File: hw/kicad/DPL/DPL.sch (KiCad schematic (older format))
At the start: 1 part

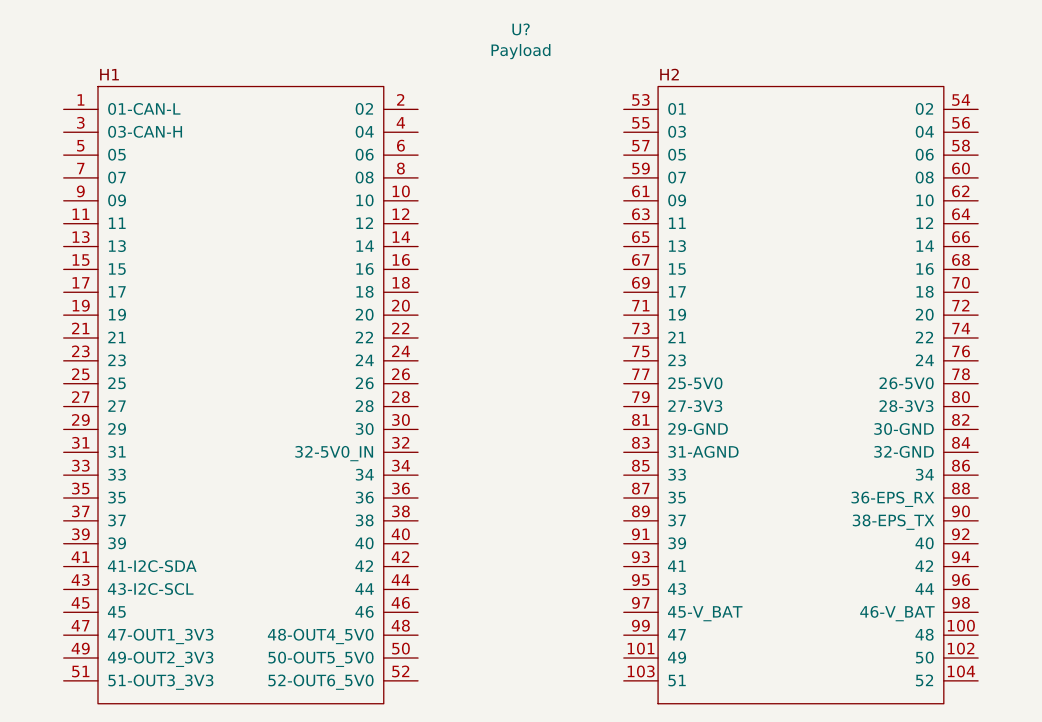
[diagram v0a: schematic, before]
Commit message: Added some net names.
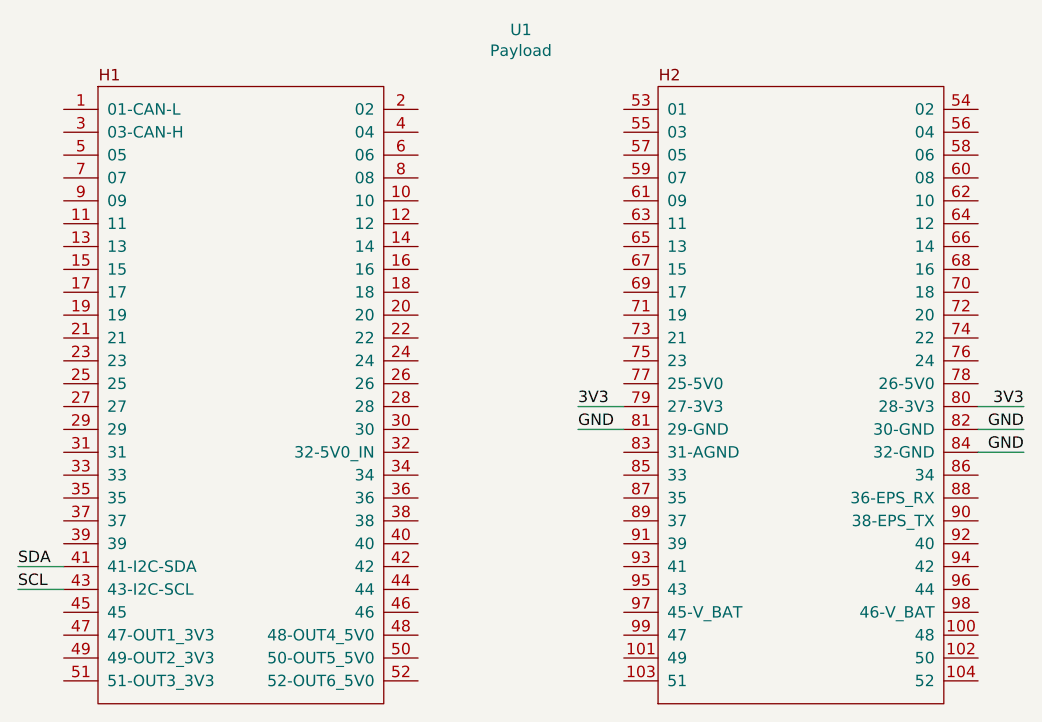
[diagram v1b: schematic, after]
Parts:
- gave numbers to parts that had none: 1
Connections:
- net SDA: now reaches U1.41 (41-I2C-SDA)
- net SCL: now reaches U1.43 (43-I2C-SCL)
- net 3V3: now reaches U1.79 (27-3V3)
- net 3V3: now also U1.80 (28-3V3)
- net GND: now reaches U1.81 (29-GND)
- net GND: now also U1.82 (30-GND), U1.84 (32-GND)
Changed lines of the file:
@@
 EESchema Schematic File Version 4
+LIBS:DPL-cache
 EELAYER 29 0
 EELAYER END
@@
 $EndDescr
 $Comp
-L Payload:Payload U?
+L Payload:Payload U1
 U 1 1 5C059BEE
 P 5950 3250
-F 0 "U?" H 5950 4798 50  0000 C CNN
+F 0 "U1" H 5950 4798 50  0000 C CNN
 F 1 "Payload" H 5950 4707 50  0000 C CNN
 F 2 "" H 4850 4050 50  0001 C CNN
@@
 	1    0    0    -1
 $EndComp
+Text Label 6200 3450 0    50   ~ 0
+GND
+Text Label 8150 3450 2    50   ~ 0
+GND
+Text Label 8150 3550 2    50   ~ 0
+GND
+Wire Wire Line
+	8150 3450 7950 3450
+Wire Wire Line
+	7950 3550 8150 3550
+Wire Wire Line
+	6400 3450 6200 3450
+Text Label 6200 3350 0    50   ~ 0
+3V3
+Text Label 8150 3350 2    50   ~ 0
+3V3
+Wire Wire Line
+	8150 3350 7950 3350
+Wire Wire Line
+	6400 3350 6200 3350
+Text Label 3750 4050 0    50   ~ 0
+SDA
+Text Label 3750 4150 0    50   ~ 0
+SCL
+Wire Wire Line
+	3950 4050 3750 4050
+Wire Wire Line
+	3750 4150 3950 4150
 $EndSCHEMATC

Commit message: Update.
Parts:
- added C? (x2): 22pF, symbol Device:C
- added C?: 100nF, symbol Device:C
- added J?: DPL1, symbol Connector:Screw_Terminal_01x02
- added J?: DPL2, symbol Connector:Screw_Terminal_01x02
- added J?: DPL3, symbol Connector:Screw_Terminal_01x02
- added J?: DPL4, symbol Connector:Screw_Terminal_01x02
- added J?: DPL5, symbol Connector:Screw_Terminal_01x02
- added J?: DPL6, symbol Connector:Screw_Terminal_01x02
- added R?: 10k, symbol Device:R
- added U?: ATmega328-PU, Package_DIP:DIP-28_W7.62mm, symbol MCU_Microchip_ATmega:ATmega328-PU
- added Y?: 8MHz, symbol Device:Crystal
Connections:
- net 3V3: now also R?.1, U?.20 (AVCC), U?.7 (VCC)
- net GND: now also C?.2, C?.2, J?.2 (Pin_2), J?.2 (Pin_2), J?.2 (Pin_2), J?.2 (Pin_2), J?.2 (Pin_2), J?.2 (Pin_2), U?.22 (GND), U?.8 (GND)
- new net DTR: C?.2
- new net MISO: U?.18 (PB4)
- new net MOSI: U?.17 (PB3)
- new net RESET: C?.1, R?.2, U?.1 (~RESET~/PC6)
- new net SCK: U?.19 (PB5)
- new net XTAL1: C?.1, U?.9 (XTAL1/PB6), Y?.2
- new net XTAL2: C?.1, U?.10 (XTAL2/PB7), Y?.1
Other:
- moved on the sheet: U1

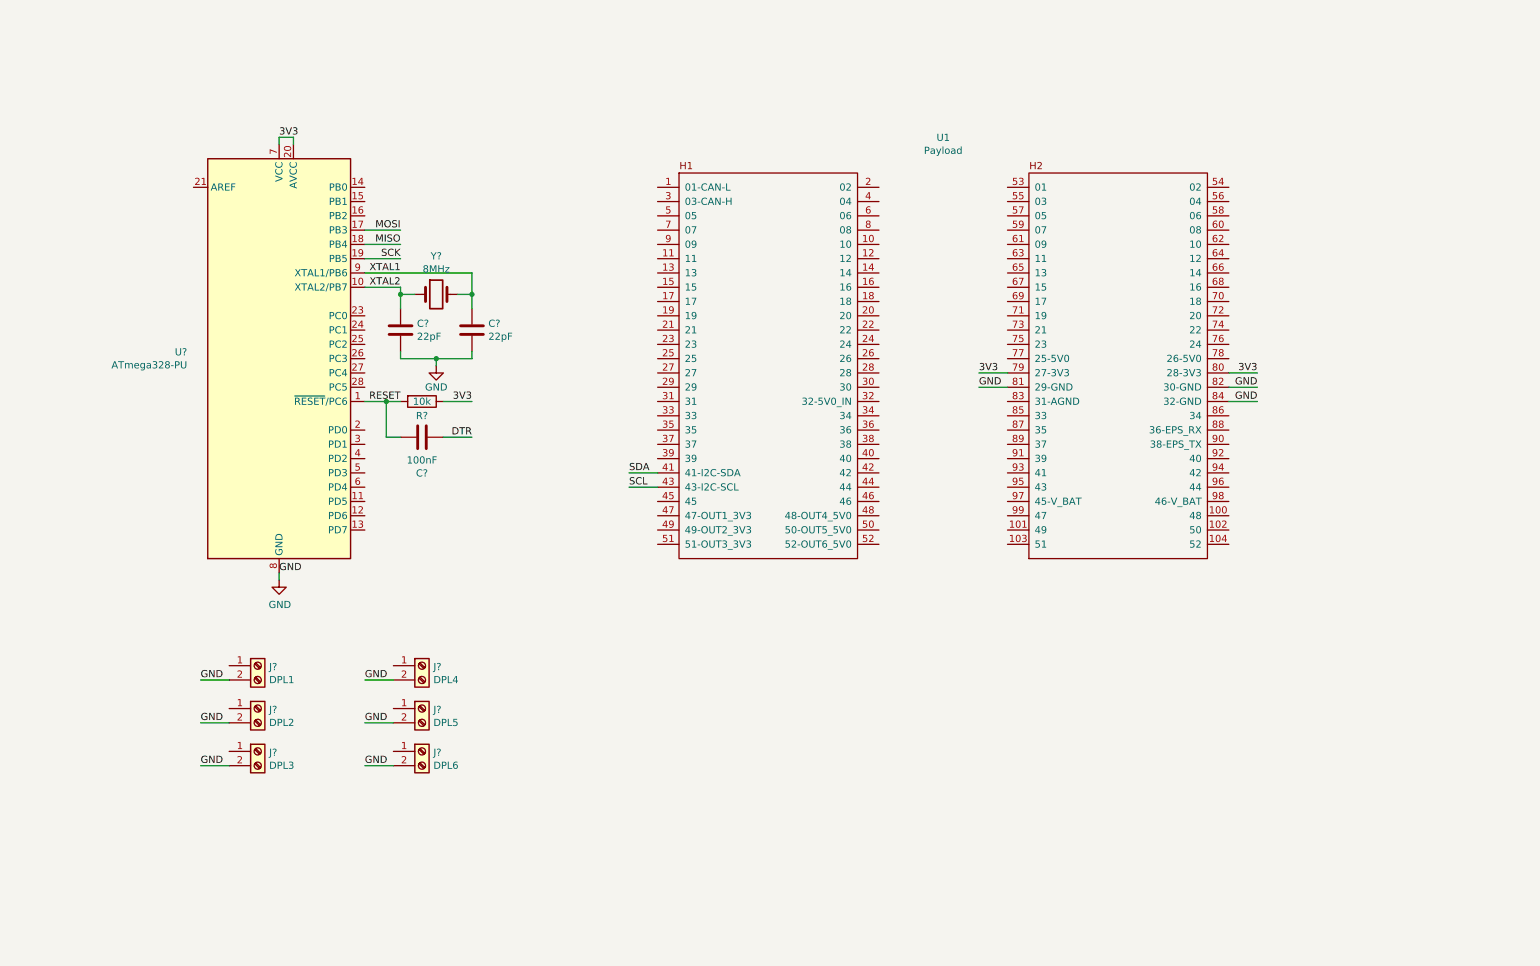
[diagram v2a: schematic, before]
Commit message: Changed the ATMEGA328 with the SAMD21E.
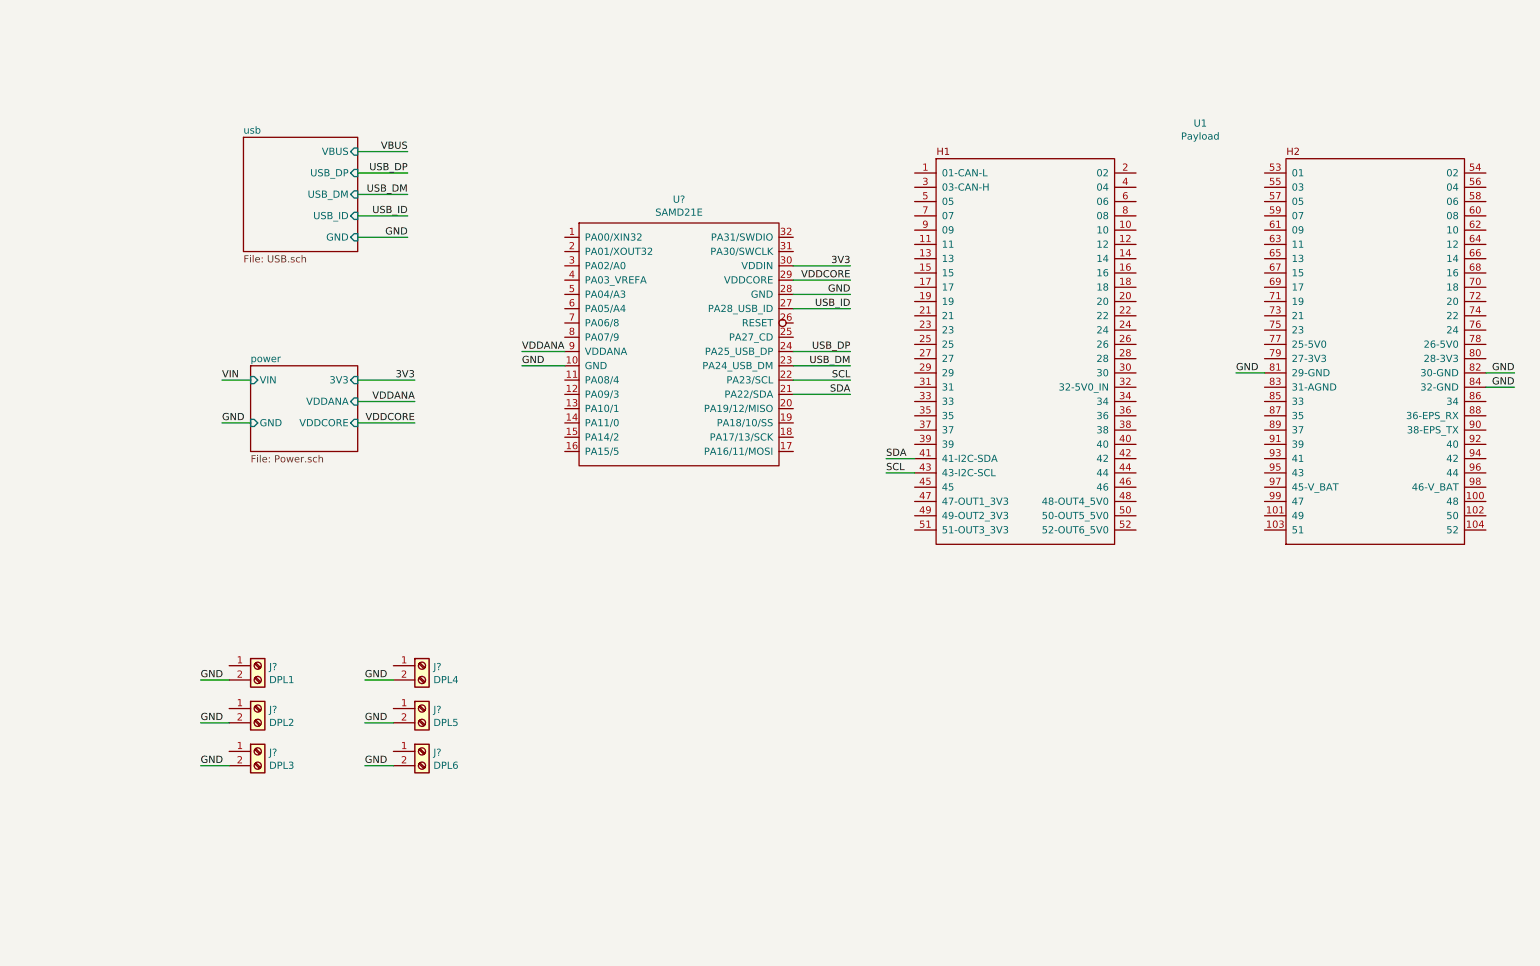
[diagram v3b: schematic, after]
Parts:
- removed C? (x2): 22pF, symbol Device:C
- removed C?: 100nF, symbol Device:C
- removed R?: 10k, symbol Device:R
- removed U?: ATmega328-PU, Package_DIP:DIP-28_W7.62mm, symbol MCU_Microchip_ATmega:ATmega328-PU
- removed Y?: 8MHz, symbol Device:Crystal
- added U?: SAMD21E, symbol Arduino:SAMD21E
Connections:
- net 3V3: now also U?.30 (VDDIN); no longer U1.79 (27-3V3), U1.80 (28-3V3)
- net GND: now also U?.10 (GND), U?.28 (GND)
- net SCL: now also U?.22 (PA23/SCL)
- net SDA: now also U?.21 (PA22/SDA)
- new net USB_DM: U?.23 (PA24_USB_DM)
- new net USB_DP: U?.24 (PA25_USB_DP)
- new net USB_ID: U?.27 (PA28_USB_ID)
- new net VDDANA: U?.9 (VDDANA)
- new net VDDCORE: U?.29 (VDDCORE)
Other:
- moved on the sheet: U1

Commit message: Added transistors for the deployment system. Updated the microcontroller's symbol.
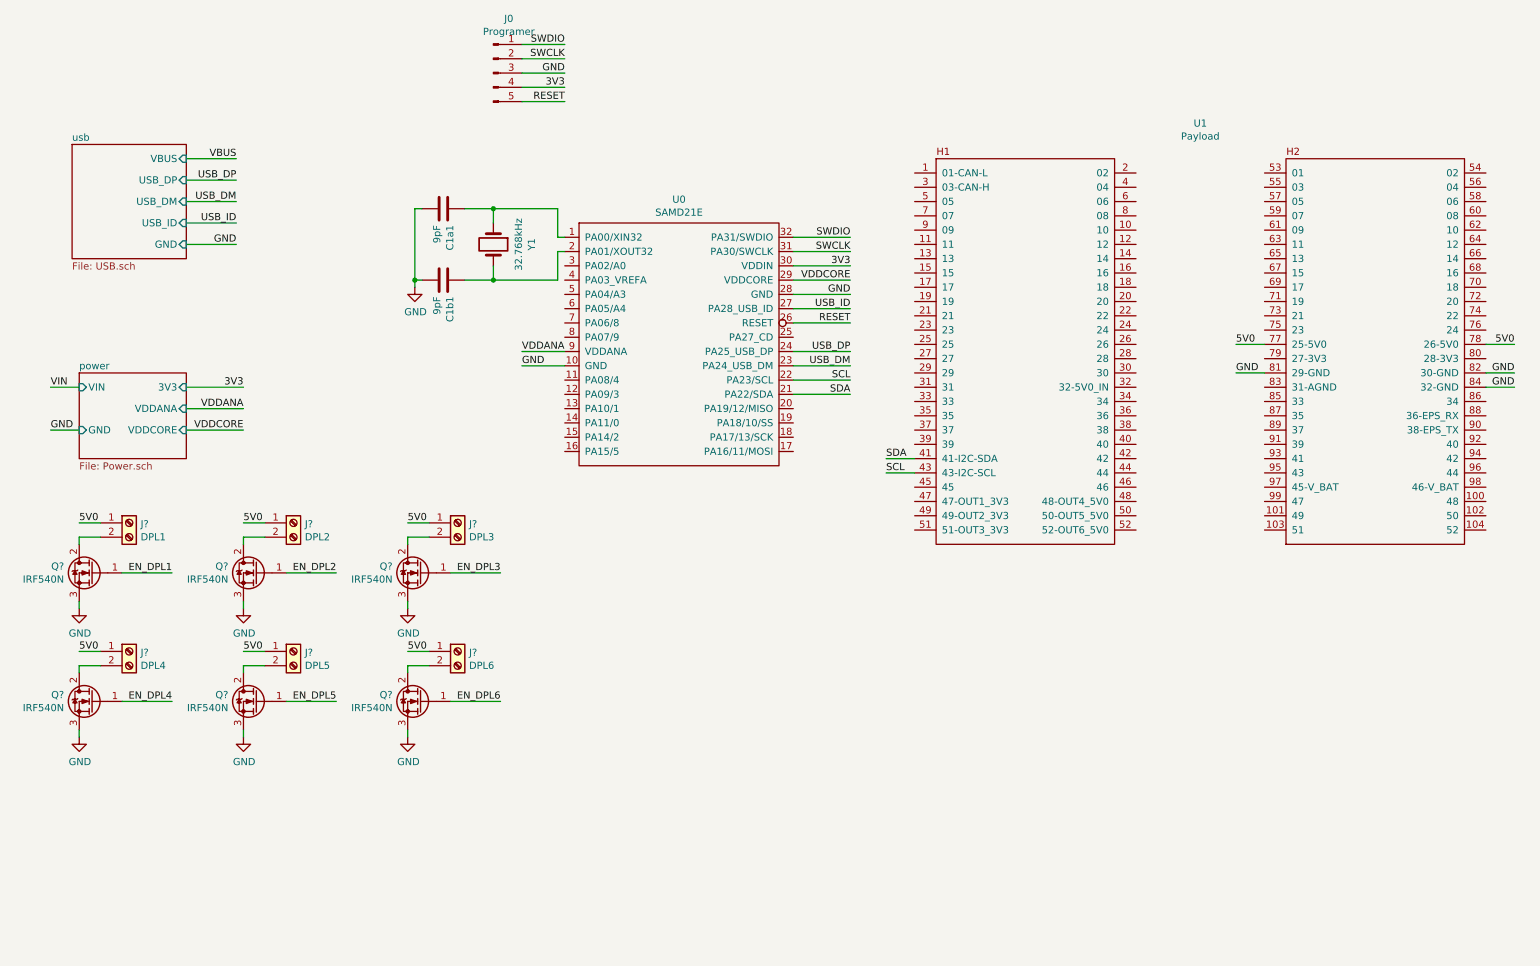
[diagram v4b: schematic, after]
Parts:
- removed U?: SAMD21E, symbol Arduino:SAMD21E
- added C1a1, C1b1: 9pF, symbol Device:C
- added J0: Programer, symbol Connector:Conn_01x05_Male
- added Q? (x6): IRF540N, Package_TO_SOT_THT:TO-220-3_Vertical, symbol Transistor_FET:IRF540N
- added U0: SAMD21E, symbol Arduino:SAMD21E
- added Y1: 32.768kHz, symbol Device:Crystal
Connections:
- net 3V3: now also J0.4 (Pin_4), U0.30 (VDDIN)
- net GND: now also C1a1.2, C1b1.2, J0.3 (Pin_3), Q?.3 (S), Q?.3 (S), Q?.3 (S), Q?.3 (S), Q?.3 (S), Q?.3 (S), U0.10 (GND), U0.28 (GND); no longer J?.2 (Pin_2), J?.2 (Pin_2), J?.2 (Pin_2), J?.2 (Pin_2), J?.2 (Pin_2), J?.2 (Pin_2)
- net SCL: now also U0.22 (PA23/SCL)
- net SDA: now also U0.21 (PA22/SDA)
- net USB_DM: now also U0.23 (PA24_USB_DM)
- net USB_DP: now also U0.24 (PA25_USB_DP)
- net USB_ID: now also U0.27 (PA28_USB_ID)
- net VDDANA: now also U0.9 (VDDANA)
- net VDDCORE: now also U0.29 (VDDCORE)
- net 5V0: now reaches U1.77 (25-5V0)
- net 5V0: now also J?.1 (Pin_1), J?.1 (Pin_1), J?.1 (Pin_1), J?.1 (Pin_1), J?.1 (Pin_1), J?.1 (Pin_1), U1.78 (26-5V0)
- new net: J?.2 (Pin_2), Q?.2 (D) (x6)
- new net: C1a1.1, U0.1 (PA00/XIN32), Y1.1
- new net: C1b1.1, U0.2 (PA01/XOUT32), Y1.2
- new net EN_DPL1: Q?.1 (G)
- new net EN_DPL2: Q?.1 (G)
- new net EN_DPL3: Q?.1 (G)
- new net EN_DPL4: Q?.1 (G)
- new net EN_DPL5: Q?.1 (G)
- new net EN_DPL6: Q?.1 (G)
- new net RESET: J0.5 (Pin_5), U0.26 (RESET)
- new net SWCLK: J0.2 (Pin_2), U0.31 (PA30/SWCLK)
- new net SWDIO: J0.1 (Pin_1), U0.32 (PA31/SWDIO)
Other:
- moved on the sheet: J?

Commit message: Added reed switches to the schematic.
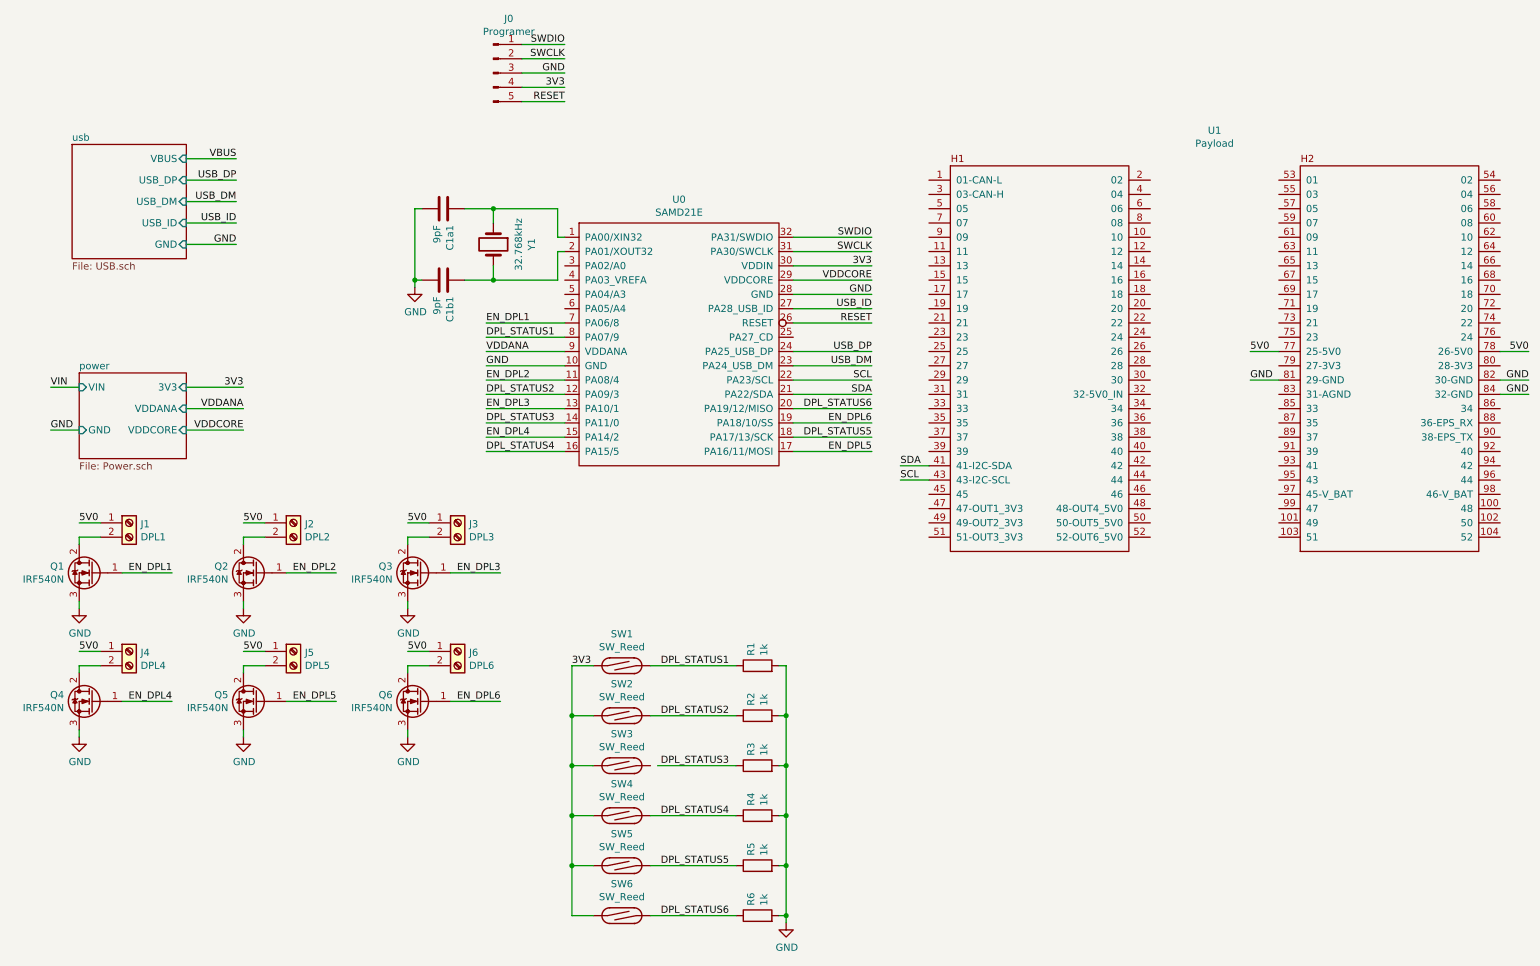
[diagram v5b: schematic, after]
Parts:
- added R1, R2, R3, R4, R5, R6: 1k, symbol Device:R
- added SW1, SW2, SW3, SW4, SW5, SW6: SW_Reed, symbol Switch:SW_Reed
- gave numbers to parts that had none: 12
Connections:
- net 3V3: now also SW1.1, SW2.1, SW3.1, SW4.1, SW5.1, SW6.1
- net EN_DPL1: now also U0.7 (PA06/8)
- net EN_DPL2: now also U0.11 (PA08/4)
- net EN_DPL3: now also U0.13 (PA10/1)
- net EN_DPL4: now also U0.15 (PA14/2)
- net EN_DPL5: now also U0.17 (PA16/11/MOSI)
- net EN_DPL6: now also U0.19 (PA18/10/SS)
- net GND: now also R1.2, R2.2, R3.2, R4.2, R5.2, R6.2
- net DPL_STATUS2: now reaches U0.12 (PA09/3)
- net DPL_STATUS2: now also R2.1, SW2.2
- net DPL_STATUS3: now reaches U0.14 (PA11/0)
- net DPL_STATUS3: now also R3.1
- net DPL_STATUS4: now reaches U0.16 (PA15/5)
- net DPL_STATUS4: now also R4.1, SW4.2
- net DPL_STATUS5: now reaches U0.18 (PA17/13/SCK)
- net DPL_STATUS5: now also R5.1, SW5.2
- net DPL_STATUS6: now reaches U0.20 (PA19/12/MISO)
- net DPL_STATUS6: now also R6.1, SW6.2
- net DPL_STATUS1: now reaches U0.8 (PA07/9)
- net DPL_STATUS1: now also R1.1, SW1.2
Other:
- moved on the sheet: U1
